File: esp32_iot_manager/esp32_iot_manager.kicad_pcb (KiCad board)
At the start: 4 copper layers, 81 x 55.2 mm, 89 parts, among them J1 SS-52400-002, J2 B2B-PH-SM4-TB, J3 GSD090012SEU, J4 Conn_01x04_Pin, J5 Conn_01x05_Pin, Q1 TEMT6000X01, Q2 BC817, Q3 BC817, U1 MCP73871, U2 BME280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

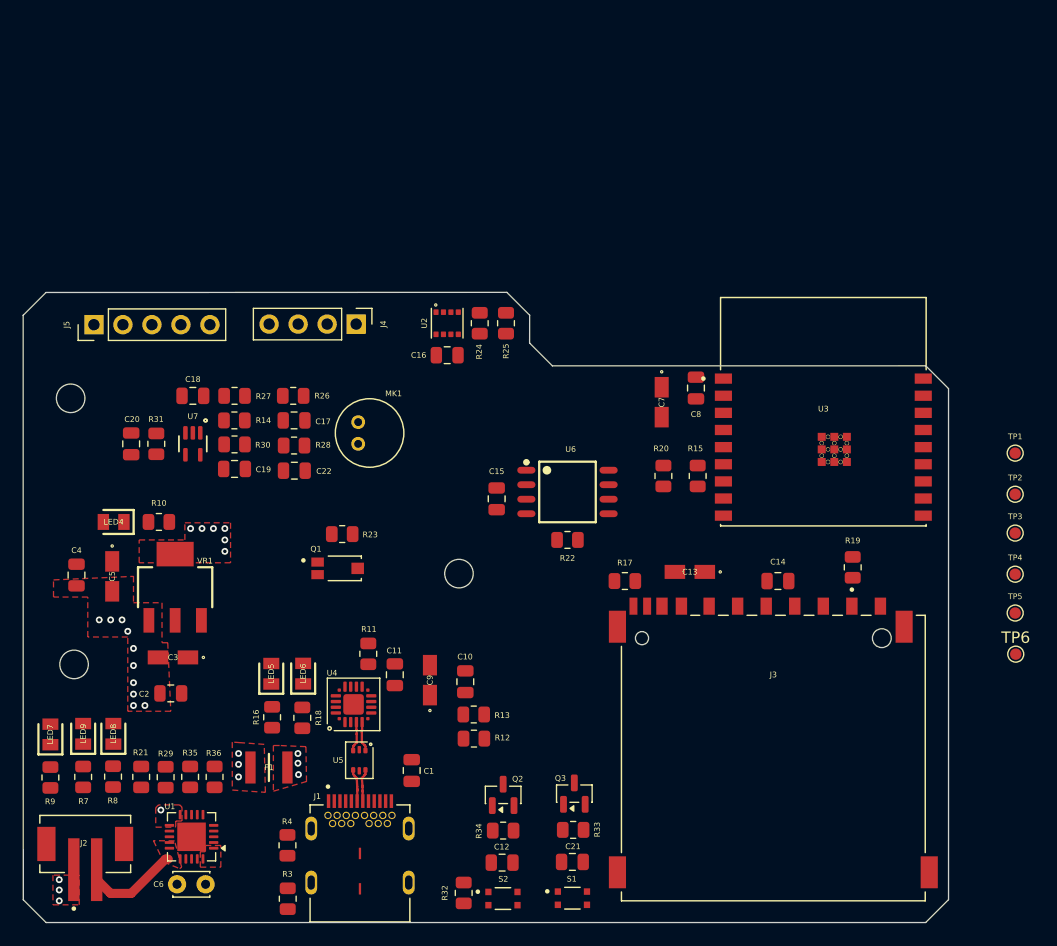
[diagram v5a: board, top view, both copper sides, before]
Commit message: routed power, gnd lines
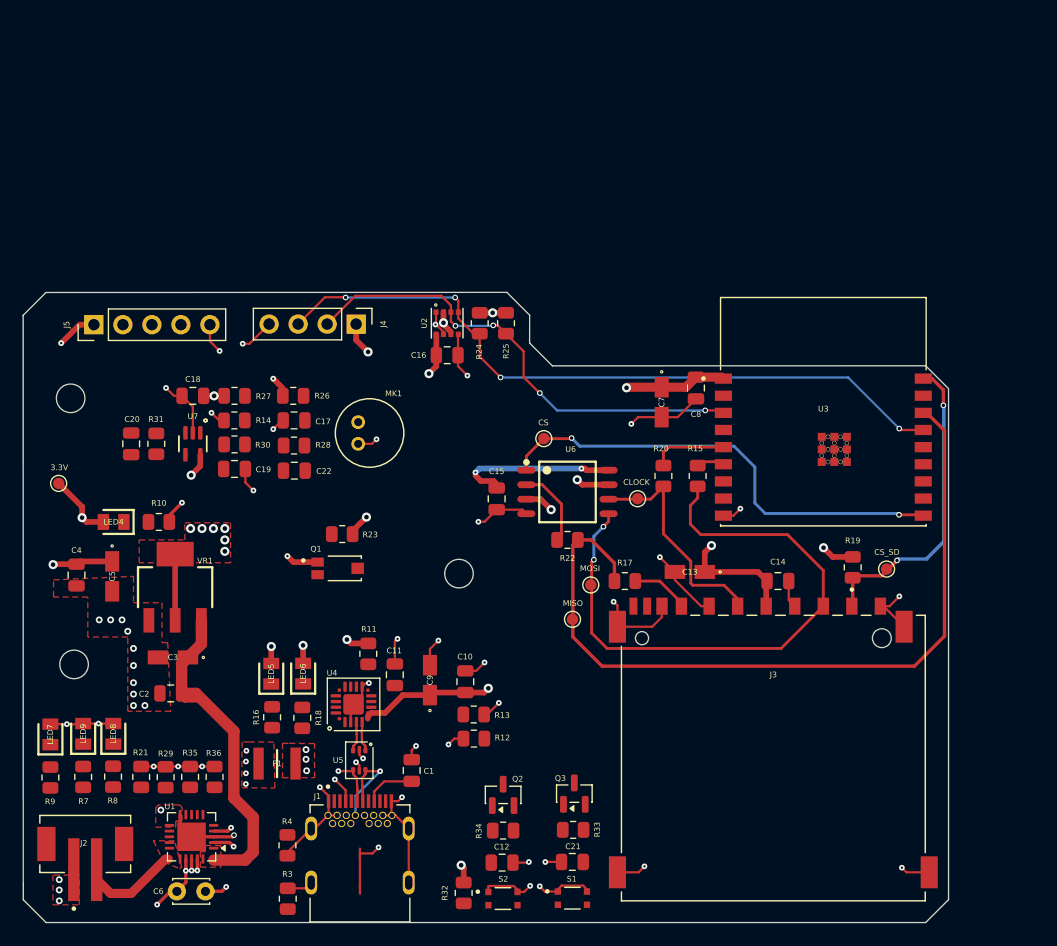
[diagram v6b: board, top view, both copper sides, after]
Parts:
- TP1: value Test MOSI -> MOSI
- TP2: value Test MISO -> MISO
- TP3: value Test clock -> CLOCK
- TP4: value Test CS -> CS
- TP5: value Test CS_SD -> CS_SD
- TP6: value Test 3.3V -> 3.3V
- moved TP6 85.1 mm to (140.4, 76.0)
- moved TP4 42.9 mm to (182.9, 72.1)
- moved TP2 40.3 mm to (185.4, 88.0)
- moved TP1 38.9 mm to (187.0, 84.9)
- moved TP3 33.2 mm to (191.1, 77.4)
- moved TP5 11.9 mm to (212.9, 83.5)
- moved F1 0.79 mm to (159.6, 100.6)
- moved C6 0.62 mm to (150.8, 111.8)
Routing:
- net GND: track 0.00 -> 136.0 mm, vias 14 -> 52
- net 3.3V: track 0.00 -> 85.7 mm, vias 6 -> 27
- net /ESP32-C3-02/MISO_DO: track 0.00 -> 69.5 mm
- net /ESP32-C3-02/SCL: track 0.00 -> 62.6 mm, vias 0 -> 4
- net /ESP32-C3-02/MOSI_DI: track 0.00 -> 53.5 mm, vias 0 -> 2
- net /ESP32-C3-02/SDA: track 0.00 -> 42.2 mm, vias 0 -> 4
- net /ESP32-C3-02/CS: track 0.00 -> 41.3 mm, vias 0 -> 2
- net +5V: track 0.00 -> 29.5 mm
- net /ESP32-C3-02/CS_SD: track 0.00 -> 27.3 mm, vias 0 -> 2
- net /ESP32-C3-02/SCLK: track 0.00 -> 20.0 mm
- net /+5V_USB: track 0.00 -> 16.5 mm, vias 3 -> 12
- net Net-(U6-VCC): track 0.00 -> 14.6 mm, vias 0 -> 2
- net /VBUS: track 0.00 -> 9.19 mm, vias 3 -> 6
- net Net-(U6-DO(IO1)): track 0.00 -> 7.08 mm
- net Net-(U3-IO6): track 0.00 -> 6.61 mm
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
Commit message: signal routing 1 error
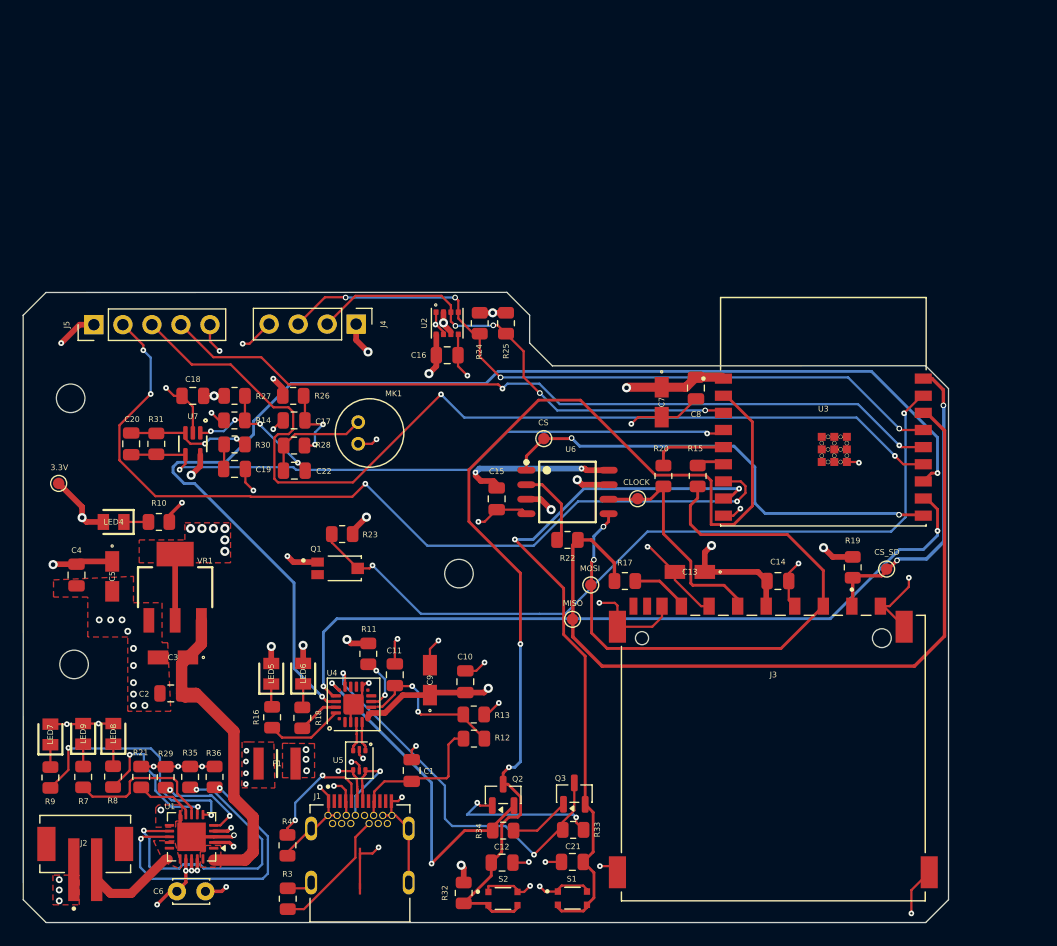
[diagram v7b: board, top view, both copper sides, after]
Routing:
- net /ESP32-C3-02/TX_RX: track 0.00 -> 105.6 mm, vias 0 -> 2
- net /ESP32-C3-02/EN: track 0.00 -> 95.3 mm, vias 0 -> 2
- net /ESP32-C3-02/GPIO18: track 0.00 -> 85.3 mm, vias 0 -> 2
- net /ESP32-C3-02/GPIO8: track 0.00 -> 77.5 mm, vias 0 -> 4
- net /ESP32-C3-02/GPI019: track 0.00 -> 69.8 mm, vias 0 -> 2
- net /ESP32-C3-02/PHOTO_C: track 0.00 -> 68.7 mm, vias 0 -> 2
- net /ESP32-C3-02/RX_TX: track 0.00 -> 67.4 mm, vias 0 -> 2
- net /ESP32-C3-02/BOOT: track 0.00 -> 62.3 mm, vias 0 -> 2
- net /ESP32-C3-02/MIC_OUT: track 0.00 -> 55.7 mm, vias 0 -> 2
- net /ESP32-C3-02/DTR: track 0.00 -> 34.8 mm, vias 0 -> 2
- net /ESP32-C3-02/RTS: track 0.00 -> 29.8 mm, vias 0 -> 2
- net Net-(U1-PROG1): track 0.00 -> 26.6 mm, vias 0 -> 2
- net Net-(U1-PROG3): track 0.00 -> 26.5 mm, vias 0 -> 2
- net Net-(U1-~{PG}): track 0.00 -> 22.2 mm, vias 0 -> 2
- net Net-(Q2-B): track 0.00 -> 13.9 mm, vias 0 -> 2
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
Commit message: finish routinh
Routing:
- net /VBUS: vias 5 -> 6
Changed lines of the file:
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@@
 	(segment
 		(start 171.36 102.14)
-		(end 168.97 102.14)
+		(end 169.53 102.14)
 		(width 0.2)
 		(layer "F.Cu")
@@
 	)
 	(segment
+		(start 169.53 102.14)
+		(end 168.97 102.14)
+		(width 0.2)
+		(layer "F.Cu")
+		(net 2)
+	)
+	(segment
 		(start 175.093 98.397)
 		(end 174.58 98.91)
@@
 		(size 0.5)
 		(drill 0.2)
+		(layers "F.Cu" "B.Cu")
+		(net 2)
+	)
+	(via
+		(at 169.53 102.14)
+		(size 0.5)
+		(drill 0.2)
